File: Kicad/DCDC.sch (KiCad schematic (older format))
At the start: 3 parts, among them IC1 MAX8881EUT33-T

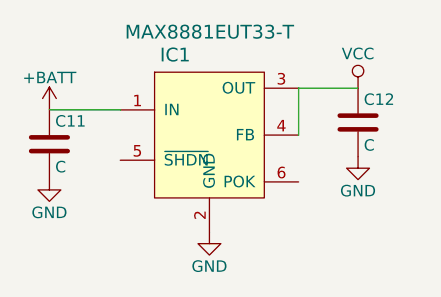
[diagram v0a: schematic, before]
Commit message: Se inició con el Pcb. Se eliminó el capacitor del socket del nrf. Se cambió el conector de la bat.
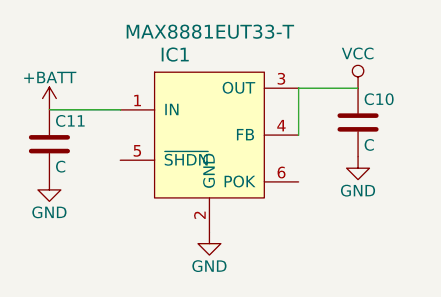
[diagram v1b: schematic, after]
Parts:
- renumbered C12 to C10
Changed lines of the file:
@@
 	5590 3445 5590 3650
 $Comp
-L C C12
+L C C10
 U 1 1 57FAEFB7
 P 5850 3595
-F 0 "C12" H 5875 3695 50  0000 L CNN
+F 0 "C10" H 5875 3695 50  0000 L CNN
 F 1 "C" H 5875 3495 50  0000 L CNN
 F 2 "EMG:C_0805" H 5888 3445 50  0001 C CNN

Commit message: Versión unificada
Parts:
- C10, C11: footprint EMG:C_0805 -> EMG:C_0603
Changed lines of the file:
@@
 F 0 "C10" H 5875 3695 50  0000 L CNN
 F 1 "C" H 5875 3495 50  0000 L CNN
-F 2 "EMG:C_0805" H 5888 3445 50  0001 C CNN
+F 2 "EMG:C_0603" H 5888 3445 50  0001 C CNN
 F 3 "" H 5850 3595 50  0000 C CNN
 	1    5850 3595
@@
 F 0 "C11" H 4525 3790 50  0000 L CNN
 F 1 "C" H 4525 3590 50  0000 L CNN
-F 2 "EMG:C_0805" H 4538 3540 50  0001 C CNN
+F 2 "EMG:C_0603" H 4538 3540 50  0001 C CNN
 F 3 "" H 4500 3690 50  0000 C CNN
 	1    4500 3690

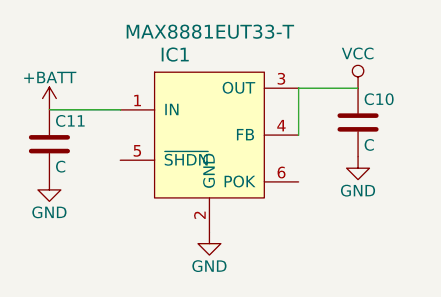
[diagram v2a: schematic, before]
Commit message: Conexión de /SHDN a IN del DC/DC
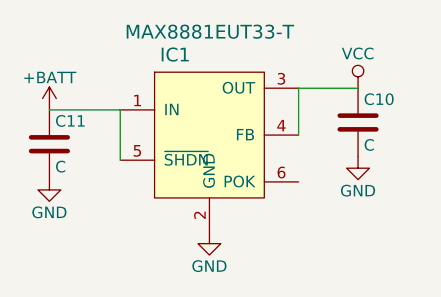
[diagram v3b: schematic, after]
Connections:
- net +BATT: now also IC1.5 (~SHDN~)
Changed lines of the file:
@@
 $EndComp
 Wire Wire Line
-	4810 3540 4500 3540
+	4500 3540 4810 3540
+Wire Wire Line
+	4810 3540 4810 3760
 $EndSCHEMATC

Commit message: Se cambia la datasheet del usb. Se agrega los step y wrl del nrf.
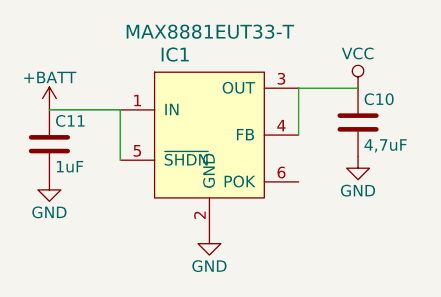
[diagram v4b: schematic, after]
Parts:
- C10: value C -> 4,7uF
- C11: value C -> 1uF
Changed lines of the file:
@@
 P 5850 3595
 F 0 "C10" H 5875 3695 50  0000 L CNN
-F 1 "C" H 5875 3495 50  0000 L CNN
+F 1 "4,7uF" H 5875 3495 50  0000 L CNN
 F 2 "EMG:C_0603" H 5888 3445 50  0001 C CNN
 F 3 "" H 5850 3595 50  0000 C CNN
@@
 P 4500 3690
 F 0 "C11" H 4525 3790 50  0000 L CNN
-F 1 "C" H 4525 3590 50  0000 L CNN
+F 1 "1uF" H 4525 3590 50  0000 L CNN
 F 2 "EMG:C_0603" H 4538 3540 50  0001 C CNN
 F 3 "" H 4500 3690 50  0000 C CNN
